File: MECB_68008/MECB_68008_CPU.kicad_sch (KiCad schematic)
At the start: 27 parts, among them J1 MECB_64AC, SW1 SW_DIP_PB, U1 ATF22V10C-15PU, U2 SST39SF040, U3 MC68008FN, U4 TC1232CPA, U5 GAL22V10, U6 AS6C4008-55, U7 74LS73, Y1 8 MHz

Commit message: Updates
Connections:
- net ~{VPA} is gone; now on net ECB_IORQ: U3.43 (~{VPA}), U7.3 (K), U7.8 (~{Q})
- net ECB_IORQ: no longer U7.13 (~{Q})
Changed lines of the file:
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@@
 		(color 0 0 0 0)
 	)
+	(junction
+		(at 255.27 147.32)
+		(diameter 0)
+		(color 0 0 0 0)
+	)
 	(no_connect
 		(at 31.75 78.74)
@@
 	(wire
 		(pts
+			(xy 266.7 152.4) (xy 255.27 152.4)
+		)
+		(stroke
+			(width 0)
+			(type default)
+		)
+	)
+	(wire
+		(pts
 			(xy 227.33 40.64) (xy 237.49 40.64)
 		)
@@
 	(wire
 		(pts
+			(xy 255.27 152.4) (xy 255.27 147.32)
+		)
+		(stroke
+			(width 0)
+			(type default)
+		)
+	)
+	(wire
+		(pts
 			(xy 262.89 35.56) (xy 274.32 35.56)
 		)
@@
 		)
 	)
-	(global_label "ECB_IORQ"
-		(shape output)
-		(at 273.05 133.35 0)
-		(fields_autoplaced yes)
-		(effects
-			(font
-				(size 1.27 1.27)
-			)
-			(justify left)
-		)
-		(property "Intersheetrefs" "${INTERSHEET_REFS}"
-			(at 284.5734 133.35 0)
-			(effects
-				(font
-					(size 1.27 1.27)
-				)
-				(justify left)
-				(hide yes)
-			)
-		)
-	)
 	(global_label "SYS_CLK"
 		(shape output)
@@
 				(hide yes)
 			)
+		)
+	)
+	(global_label "ECB_IORQ"
+		(shape output)
+		(at 266.7 152.4 0)
+		(fields_autoplaced yes)
+		(effects
+			(font
+				(size 1.27 1.27)
+			)
+			(justify left)
+		)
+		(property "Intersheetrefs" "${INTERSHEET_REFS}"
+			(at 278.2234 152.4 0)
+			(effects
+				(font
+					(size 1.27 1.27)
+				)
+				(justify left)
+				(hide yes)
+			)

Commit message: Updated schematic
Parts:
- added JP3: Jumper_3_Open, Connector_PinHeader_2.54mm:PinHeader_1x03_P2.54mm_Vertical, symbol Jumper:Jumper_3_Open
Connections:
- net CPU_RW: no longer JP2.1 (A), U1.3 (IN_2), U3.33 (R/~{W})
- net ECB_IORQ: now also JP3.2 (C); no longer U7.3 (K), U7.8 (~{Q})
- net at U7.13 (~{Q}): now also JP3.3 (B)
- net ECB_WR renamed ~{ECB_RD}
- net ROM_RW renamed ROM_R~{W}
- new net: JP3.1 (A), U7.3 (K), U7.8 (~{Q})
- new net CPU_R~{W}: JP2.1 (A), U1.3 (IN_2), U3.33 (R/~{W})

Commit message: Updated schematic
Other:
- note removed: "Greg@DigicoolThings.com"

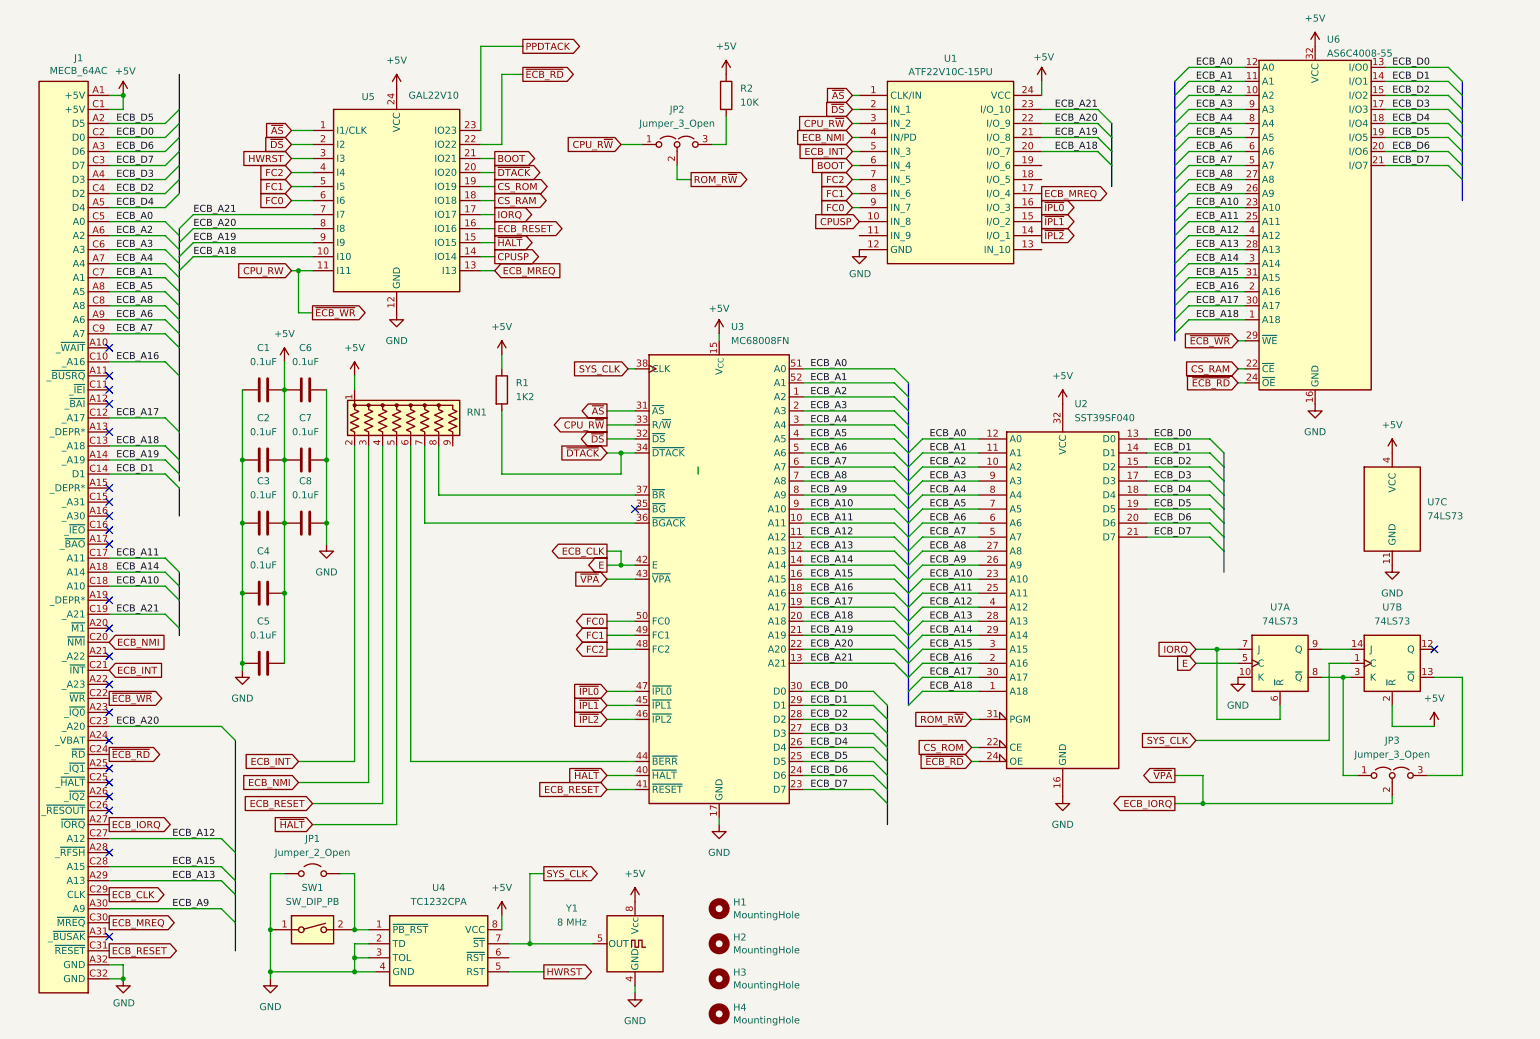
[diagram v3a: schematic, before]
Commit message: Version 0.1 of the schematic complete
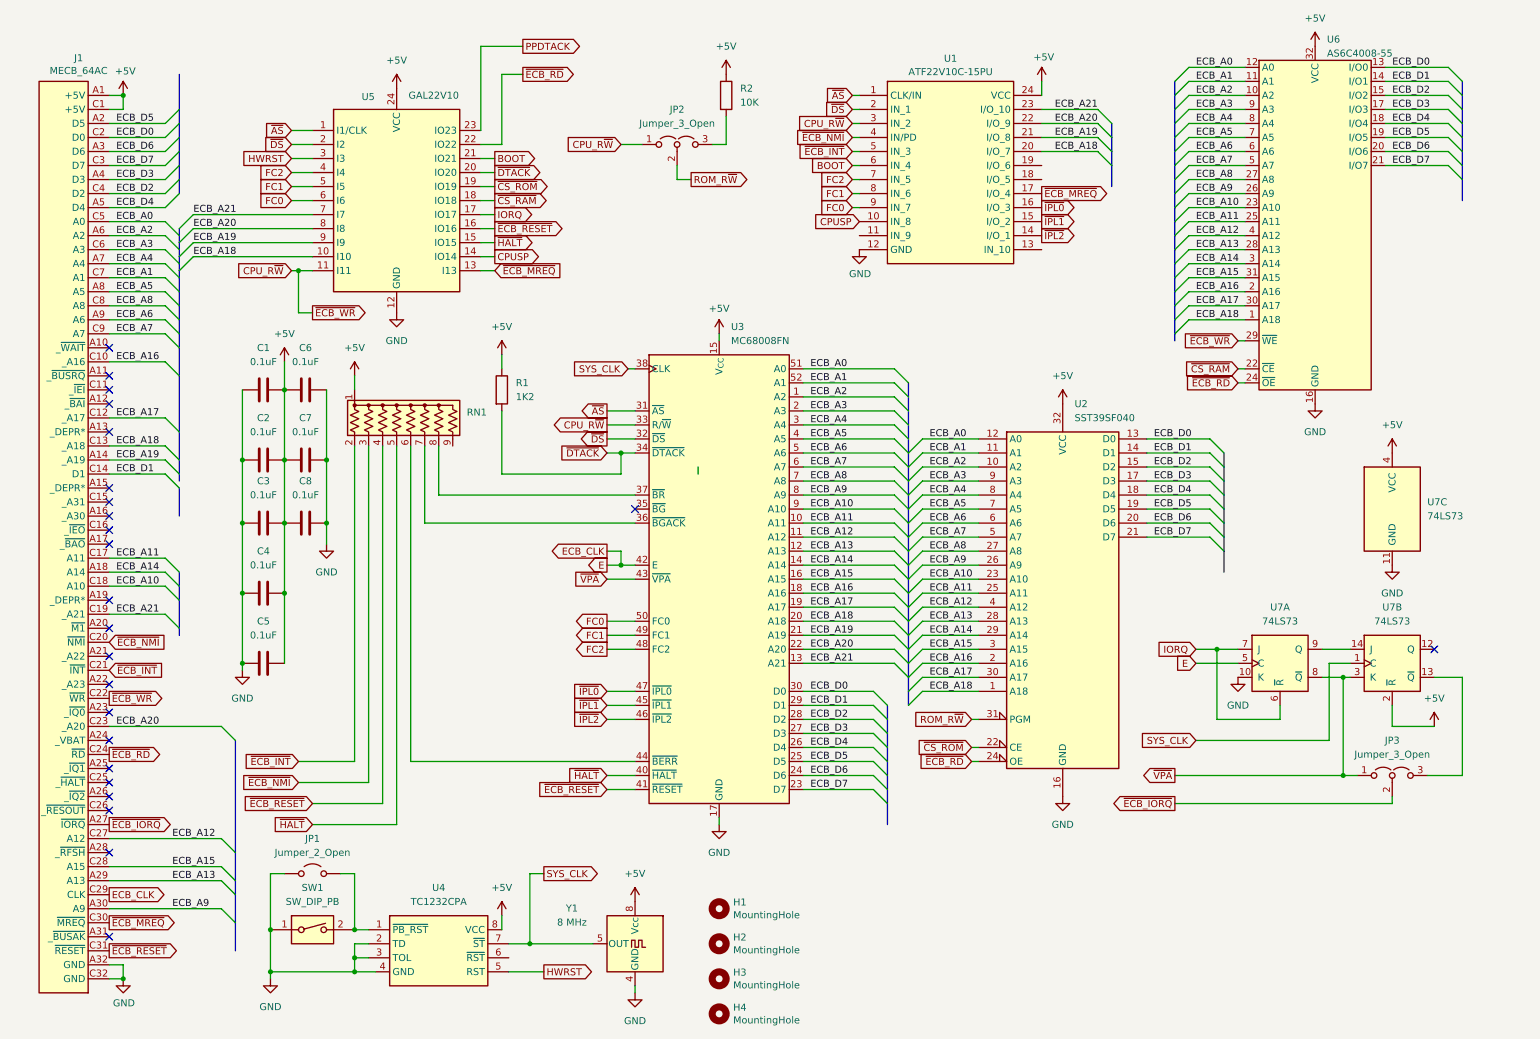
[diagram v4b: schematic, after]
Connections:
- net CPU_RW is gone; now on net CPU_R~{W}: J1.C22 (~{WR}), U5.11 (I11), U6.29 (~{WE})
- net ~{VPA}: now reaches JP3.1 (A), U7.3 (K), U7.8 (~{Q})
- net ~{VPA}: now also U3.43 (~{VPA})
- net CS_RAM renamed ~{CS_RAM}
- net CS_ROM renamed ~{CS_ROM}
- net ECB_INT renamed ~{ECB_INT}
- net ECB_IORQ renamed ~{ECB_IORQ}
- net ~{ECB_IORQ}: no longer U3.43 (~{VPA})
- net ECB_MREQ renamed ~{ECB_MREQ}
- net ECB_NMI renamed ~{ECB_NMI}
- net ECB_RESET renamed ~{ECB_RESET}
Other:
- company: DigicoolThings.com -> (none)
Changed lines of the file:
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@@
 		(title "Minimalist Europe Card Bus (MECB) 68008 Board")
 		(date "2025-05")
-		(rev "1.0")
-		(company "DigicoolThings.com")
+		(rev "0.1")
 		(comment 1 "For Minimalist Europe Card Bus (MECB). ")
 		(comment 2 "Note: CPUSP and ECB_MREQ need to be manually connected")
@@
 	)
 	(junction
+		(at 255.27 151.13)
+		(diameter 0)
+		(color 0 0 0 0)
+	)
+	(junction
 		(at 76.2 179.07)
 		(diameter 0)
@@
 	)
 	(junction
-		(at 229.87 156.21)
-		(diameter 0)
-		(color 0 0 0 0)
-	)
-	(junction
 		(at 124.46 113.03)
 		(diameter 0)
@@
 	(wire
 		(pts
-			(xy 229.87 151.13) (xy 229.87 156.21)
-		)
-		(stroke
-			(width 0)
-			(type default)
-		)
-	)
-	(wire
-		(pts
 			(xy 102.87 24.13) (xy 102.87 36.83)
 		)
@@
 		)
 	)
-	(wire
-		(pts
-			(xy 224.79 156.21) (xy 229.87 156.21)
-		)
-		(stroke
-			(width 0)
-			(type default)
-		)
-	)
 	(bus
 		(pts
@@
 	(wire
 		(pts
-			(xy 229.87 151.13) (xy 224.79 151.13)
+			(xy 224.79 151.13) (xy 255.27 151.13)
 		)
 		(stroke
@@
 	(wire
 		(pts
-			(xy 264.16 156.21) (xy 229.87 156.21)
+			(xy 224.79 156.21) (xy 264.16 156.21)
 		)
 		(stroke
@@
 		)
 	)
-	(global_label "ECB_RESET"
+	(global_label "~{ECB_RESET}"
 		(shape output)
 		(at 31.75 182.88 0)
@@
 		)
 		(property "Intersheetrefs" "${INTERSHEET_REFS}"
-			(at 44.4761 182.8006 0)
+			(at 44.4827 182.88 0)
 			(effects
 				(font
@@
 		)
 	)
-	(global_label "ECB_MREQ"
+	(global_label "~{ECB_MREQ}"
 		(shape output)
 		(at 31.75 177.8 0)
@@
 		)
 		(property "Intersheetrefs" "${INTERSHEET_REFS}"
-			(at 43.9318 177.7206 0)
+			(at 43.9385 177.8 0)
 			(effects
 				(font
@@
 		)
 	)
-	(global_label "CS_RAM"
+	(global_label "~{CS_RAM}"
 		(shape output)
 		(at 101.6 46.99 0)
@@
 		)
 	)
-	(global_label "ECB_INT"
+	(global_label "~{ECB_INT}"
 		(shape input)
 		(at 31.75 132.08 0)
@@
 		)
 		(property "Intersheetrefs" "${INTERSHEET_REFS}"
-			(at 41.6337 132.0006 0)
+			(at 41.6405 132.08 0)
 			(effects
 				(font
@@
 		)
 	)
-	(global_label "ECB_MREQ"
+	(global_label "~{ECB_MREQ}"
 		(shape output)
 		(at 200.66 45.72 0)
@@
 		)
 	)
-	(global_label "ECB_RESET"
+	(global_label "~{ECB_RESET}"
 		(shape output)
 		(at 101.6 52.07 0)
@@
 		)
 	)
-	(global_label "ECB_IORQ"
+	(global_label "~{ECB_IORQ}"
 		(shape output)
 		(at 31.75 160.02 0)
@@
 		)
 		(property "Intersheetrefs" "${INTERSHEET_REFS}"
-			(at 43.2666 159.9406 0)
+			(at 43.2734 160.02 0)
 			(effects
 				(font
@@
 		)
 	)
-	(global_label "ECB_INT"
+	(global_label "~{ECB_INT}"
 		(shape input)
 		(at 166.37 38.1 180)
@@
 		)
 	)
-	(global_label "ECB_INT"
+	(global_label "~{ECB_INT}"
 		(shape input)
 		(at 66.04 148.59 180)
@@
 		)
 		(property "Intersheetrefs" "${INTERSHEET_REFS}"
-			(at 56.1563 148.5106 0)
+			(at 56.1495 148.59 0)
 			(effects
 				(font
@@
 		)
 	)
-	(global_label "CS_ROM"
+	(global_label "~{CS_ROM}"
 		(shape output)
 		(at 101.6 44.45 0)
@@
 		)
 	)
-	(global_label "ECB_RESET"
+	(global_label "~{ECB_RESET}"
 		(shape input)
 		(at 68.58 156.21 180)
@@
 		)
 	)
-	(global_label "CS_ROM"
+	(global_label "~{CS_ROM}"
 		(shape input)
 		(at 187.96 146.05 180)
@@
 		)
 	)
-	(global_label "ECB_MREQ"
+	(global_label "~{ECB_MREQ}"
 		(shape input)
 		(at 101.6 59.69 0)
@@
 		)
 	)
-	(global_label "ECB_NMI"
+	(global_label "~{ECB_NMI}"
 		(shape input)
 		(at 66.04 152.4 180)
@@
 		)
 		(property "Intersheetrefs" "${INTERSHEET_REFS}"
-			(at 55.6725 152.3206 0)
+			(at 55.6657 152.4 0)
 			(effects
 				(font
@@
 		)
 	)
-	(global_label "ECB_RESET"
+	(global_label "~{ECB_RESET}"
 		(shape input)
 		(at 121.92 153.67 180)
@@
 		)
 	)
-	(global_label "CS_RAM"
+	(global_label "~{CS_RAM}"
 		(shape input)
 		(at 236.22 77.47 180)
@@
 		)
 	)
-	(global_label "ECB_IORQ"
+	(global_label "~{ECB_IORQ}"
 		(shape output)
 		(at 224.79 156.21 180)
@@
 		)
 	)
-	(global_label "ECB_NMI"
+	(global_label "~{ECB_NMI}"
 		(shape input)
 		(at 31.75 127 0)
@@
 		)
 		(property "Intersheetrefs" "${INTERSHEET_REFS}"
-			(at 42.1175 126.9206 0)
+			(at 42.1243 127 0)
 			(effects
 				(font
@@
 		)
 	)
-	(global_label "CPU_RW"
+	(global_label "CPU_R~{W}"
 		(shape input)
 		(at 64.77 59.69 180)
@@
 		)
 	)
-	(global_label "ECB_NMI"
+	(global_label "~{ECB_NMI}"
 		(shape input)
 		(at 166.37 35.56 180)

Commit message: v1.1 board finalised
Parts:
- removed C7, C8: 0.1uF, Capacitor_THT:C_Disc_D5.0mm_W2.5mm_P2.50mm, symbol Device:C
- removed JP3: Jumper_3_Open, Connector_PinHeader_2.54mm:PinHeader_1x03_P2.54mm_Vertical, symbol Jumper:Jumper_3_Open
- removed R1: 1K2, Resistor_THT:R_Axial_DIN0309_L9.0mm_D3.2mm_P12.70mm_Horizontal, symbol Device:R
- removed U7: 74LS73, Package_DIP:DIP-14_W7.62mm_LongPads, symbol 74xx:74LS73
- C1, C2, C3, C4, C5, C6: footprint Capacitor_THT:C_Disc_D5.0mm_W2.5mm_P2.50mm -> Capacitor_THT:C_Disc_D5.0mm_W2.5mm_P5.00mm
- R1: renamed from R2; value 10K -> 4K7
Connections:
- net IORQ is gone; now on net ~{IPL2}: U5.17 (IO17)
- net ~{VPA} is gone; now on net ~{ECB_IORQ}: U3.43 (~{VPA})
- net BOOT: now also U1.3 (IN_2); no longer U1.6 (IN_4)
- net CPU_R~{W}: now also U1.9 (IN_7); no longer U1.3 (IN_2)
- net ECB_A12: now also U1.17 (I/O_4)
- net ECB_A13: now also U1.16 (I/O_3)
- net ECB_A14: now also U1.15 (I/O_2)
- net ECB_A15: now also U1.14 (I/O_1)
- net ECB_A16: now also U1.13 (IN_10)
- net ECB_A17: now also U1.11 (IN_9)
- net ECB_A18: now also U1.8 (IN_6); no longer U1.20 (I/O_7)
- net ECB_A19: now also U1.7 (IN_5); no longer U1.21 (I/O_8)
- net ECB_A20: now also U1.6 (IN_4); no longer U1.22 (I/O_9), U5.8 (I8)
- net ECB_A21: now also U1.5 (IN_3); no longer U1.23 (I/O_10), U5.7 (I7)
- net FC0: no longer U1.9 (IN_7)
- net FC1: no longer U1.8 (IN_6)
- net FC2: no longer U1.7 (IN_5)
- net PPDTACK: now also U1.23 (I/O_10); no longer U5.23 (IO23)
- net ~{CS_RAM}: now also U1.21 (I/O_8); no longer U5.18 (IO18)
- net ~{CS_ROM}: now also U1.22 (I/O_9); no longer U5.19 (IO19)
- net ~{DTACK}: now also RN1.9 (R8), U1.18 (I/O_5); no longer U5.20 (IO20)
- net ~{ECB_INT}: now also U5.7 (I7); no longer U1.5 (IN_3)
- net ~{ECB_IORQ}: now also U1.20 (I/O_7)
- net ~{ECB_MREQ}: now also U1.19 (I/O_6); no longer U1.17 (I/O_4), U5.13 (I13)
- net ~{ECB_NMI}: now also U5.8 (I8); no longer U1.4 (IN/PD)
- net ~{ECB_RESET}: now also U1.4 (IN/PD)
- net ~{IPL0}: now also U5.19 (IO19); no longer U1.16 (I/O_3)
- net ~{IPL1}: now also U5.18 (IO18); no longer U1.15 (I/O_2)
- net ~{IPL2}: no longer U1.14 (I/O_1)
- no-connect marks 24 -> 26
